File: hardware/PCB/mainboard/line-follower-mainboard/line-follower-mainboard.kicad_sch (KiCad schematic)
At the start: 29 parts, among them J1 Xt30, J2 2-Pin, J3 2-Pin, J4 8x2 Sensor connector, U2 L7805, U3 74HC164

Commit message: Created prototype sensor array schematic and PCB, revised mainboard
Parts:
- J4: footprint (none) -> Connector_PinSocket_2.54mm:PinSocket_2x08_P2.54mm_Vertical; DigiKeyPartNumber (none) -> S7111-ND

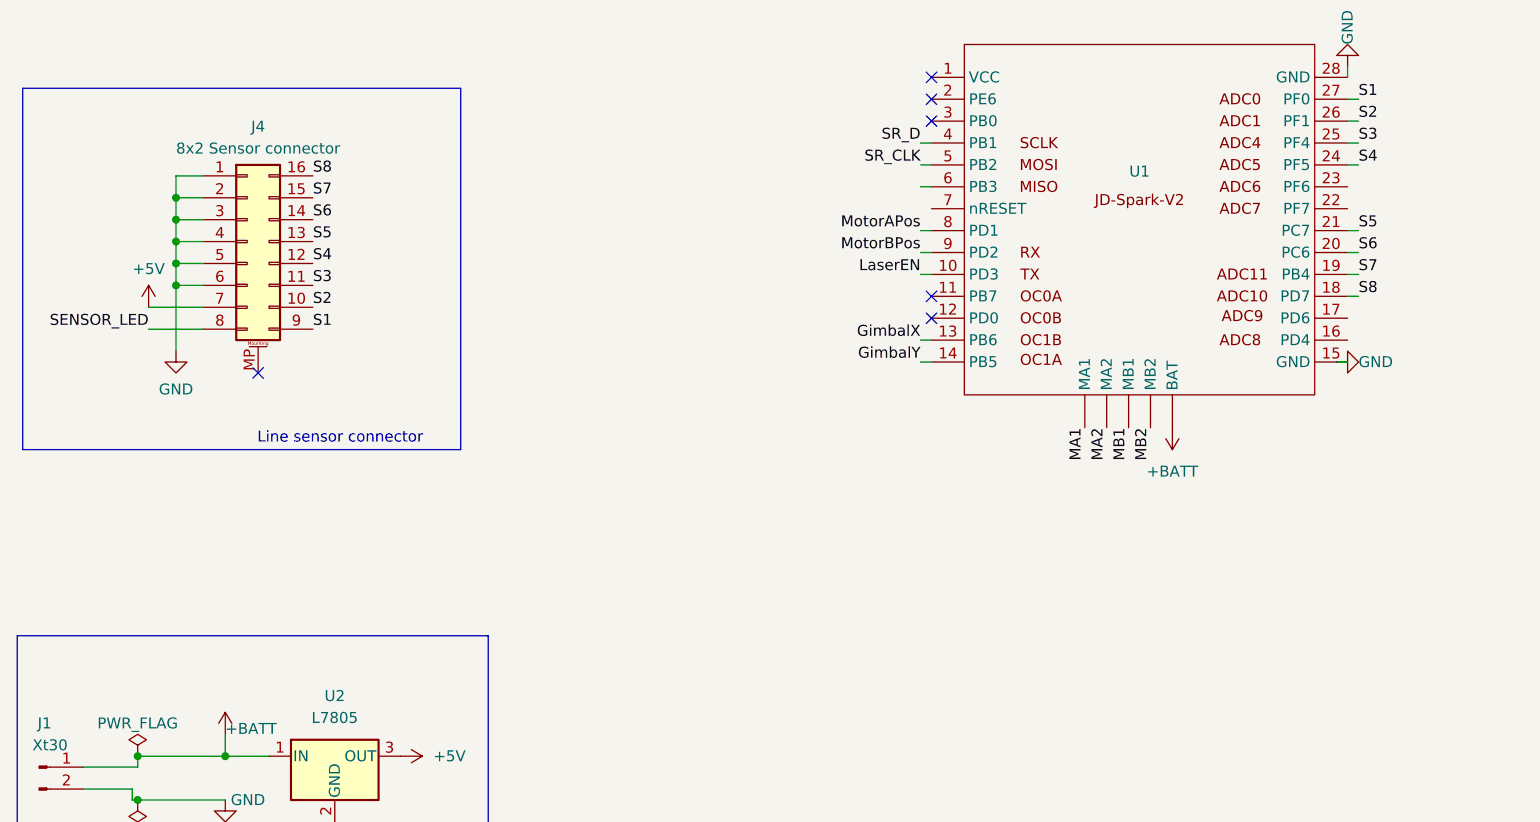
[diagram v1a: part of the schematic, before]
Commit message: Finished PCBs for payload and turret
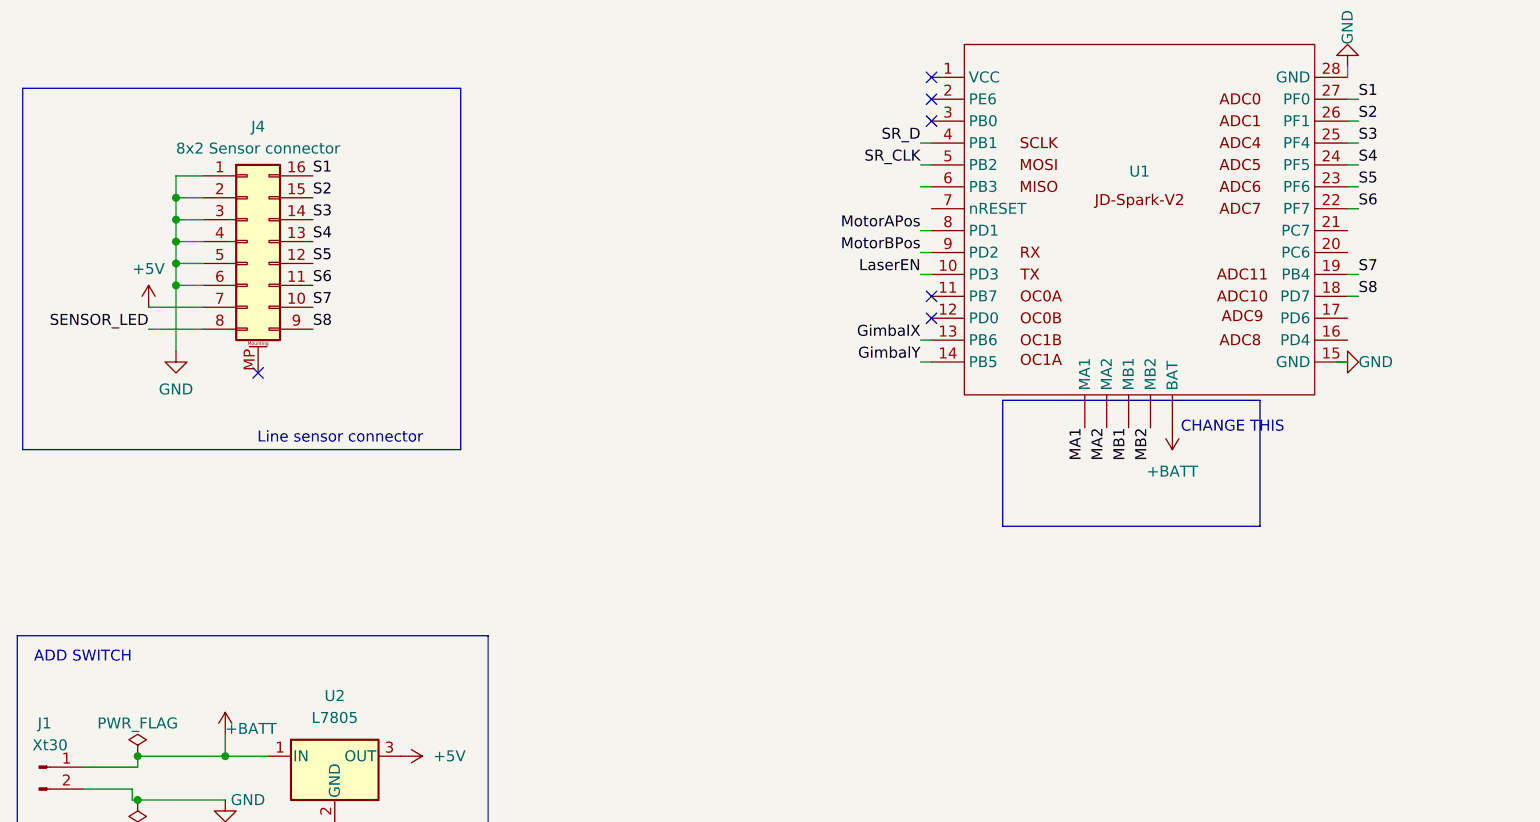
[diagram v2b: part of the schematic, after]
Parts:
- U3: DigiKeyPartNumber (none) -> 296-14838-1-ND
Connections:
- net S1: now also J4.16 (Pin_16); no longer J4.9 (Pin_9)
- net S2: now also J4.15 (Pin_15); no longer J4.10 (Pin_10)
- net S3: now also J4.14 (Pin_14); no longer J4.11 (Pin_11)
- net S4: now also J4.13 (Pin_13); no longer J4.12 (Pin_12)
- net S5: now also J4.12 (Pin_12), U1.23 (PF6); no longer J4.13 (Pin_13), U1.21 (PC7)
- net S6: now also J4.11 (Pin_11), U1.22 (PF7); no longer J4.14 (Pin_14), U1.20 (PC6)
- net S7: now also J4.10 (Pin_10); no longer J4.15 (Pin_15)
- net S8: now also J4.9 (Pin_9); no longer J4.16 (Pin_16)
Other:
- note added: "ADD SWITCH"
- note added: "CHANGE THIS"

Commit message: payload v2
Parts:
- removed D1, D10, D2, D3, D4, D7, D8, D9: 1N5817, symbol Device:D_Schottky
- removed D11, D12, D5, D6: LED, symbol Device:LED
- removed J2, J3: 2-Pin, symbol Connector:Conn_01x02_Pin
- removed R1, R2, R3: 150R, symbol Device:R
- removed U1: ~, symbol MCU_Microchip_ATmega:JD-Spark-V2
- added D4: STATUS, LED_THT:LED_D5.0mm, symbol Device:LED
- added H1, H2, H3, H4: MountingHole, MountingHole:MountingHole_3.2mm_M3_DIN965_Pad_TopBottom, symbol Mechanical:MountingHole_Pad
- added J3: linefollower->payload, Connector_PinHeader_2.54mm:PinHeader_2x08_P2.54mm_Vertical, symbol Connector_Generic:Conn_01x07
- added J4: MOTOR_B, Connector_PinHeader_2.54mm:PinHeader_1x02_P2.54mm_Vertical, symbol Connector:Screw_Terminal_01x02
- added J5: MOTOR_A, Connector_PinHeader_2.54mm:PinHeader_1x02_P2.54mm_Vertical, symbol Connector:Screw_Terminal_01x02
- added SW1: RST, symbol Switch:SW_Push
- added SW2: MODE, symbol Switch:SW_Push
- added U3: Teensy2.0_(Arduino), Library:Teensy2.0, symbol teensy:Teensy2.0_(Arduino)
- added U4: ~, Library:DRV8833, symbol Driver_Motor:DRV8833
- D1: renamed from D13; footprint (none) -> LED_THT:LED_D5.0mm
- D2: renamed from D14; footprint (none) -> LED_THT:LED_D5.0mm
- D3: renamed from D15; footprint (none) -> LED_THT:LED_D5.0mm
- J1: footprint (none) -> Connector_AMASS:AMASS_XT30PW-M_1x02_P2.50mm_Horizontal
- R1: renamed from R5; footprint (none) -> Resistor_THT:R_Axial_DIN0207_L6.3mm_D2.5mm_P7.62mm_Horizontal
- R2: renamed from R6; footprint (none) -> Resistor_THT:R_Axial_DIN0207_L6.3mm_D2.5mm_P7.62mm_Horizontal
- R3: renamed from R7; footprint (none) -> Resistor_THT:R_Axial_DIN0207_L6.3mm_D2.5mm_P7.62mm_Horizontal
- R4: value 150R -> 100; footprint (none) -> Resistor_THT:R_Axial_DIN0207_L6.3mm_D2.5mm_P7.62mm_Horizontal
- U2: renamed from U3; footprint (none) -> Library:74HC164DR
- renumbered J4 to J2, U2 to U1
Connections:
- net MB2 is gone; now on net Q3: R4.2
- net GND: now also D4.1 (K), H1.1, H2.1, H3.1, H4.1, J3.1 (Pin_1), J3.7 (Pin_7), SW1.2, SW2.1, U3.1 (GND), U3.15 (GND), U4.1 (GND), U4.9 (GND)
- net S1: now also U3.28 (21_A0)
- net S2: now also U3.27 (20_A1)
- net S3: now also U3.26 (19_A2)
- net S4: now also U3.25 (18_A3)
- net S5: now also U3.24 (17_A4)
- net S6: now also U3.23 (16_A5)
- net S7: now also U3.22 (15_A6_PWM)
- net S8: now also U3.21 (14_A7_PWM)
- net SR_CLK: now also U3.3 (1)
- net SR_D: now also U3.2 (0)
- net at R4.1: now also D4.2 (A)
- net Q3: now reaches U2.6 (Q3)
- net +5V renamed 5V
- net 5V: now also J3.2 (Pin_2), J3.6 (Pin_6), U3.14 (+5V)
- net +BATT renamed VBATT
- net VBATT: now also J3.4 (Pin_4), U4.2 (VIN)
- new net: J5.1 (Pin_1), U4.13 (AOUT2)
- new net: J5.2 (Pin_2), U4.14 (AOUT1)
- new net: SW2.2, U3.17 (22_A11)
- new net: SW1.1, U3.16 (RST)
- new net: J4.1 (Pin_1), U4.11 (BOUT1)
- new net: J4.2 (Pin_2), U4.12 (BOUT2)
- new net MOT_A1_PWM: U3.12 (10_PWM), U4.6 (AIN1)
- new net MOT_A2_PWM: U3.11 (9_PWM), U4.5 (AIN2)
- new net MOT_B1_PWM: U3.6 (4_PWM), U4.3 (BIN1)
- new net MOT_B2_PWM: U3.7 (5_INT0_PWM), U4.4 (BIN2)
- new net MOT_FLT: U3.13 (23), U4.8 (nFAULT)
- new net SZ_SIG: J3.5 (Pin_5), U3.4 (2)
- new net TRK_SIG: J3.3 (Pin_3), U3.5 (3)
- no-connect marks 6 -> 17
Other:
- note removed: "CHANGE THIS"
- note removed: "Motor A and B"

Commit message: finalised mainboard design
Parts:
- removed J2: 8x2 Sensor connector, Connector_PinSocket_2.54mm:PinSocket_2x08_P2.54mm_Vertical, symbol Connector_Generic_MountingPin:Conn_02x08_Counter_Clockwise_MountingPin
- removed SW1: RST, symbol Switch:SW_Push
- removed SW2: MODE, symbol Switch:SW_Push
- added J2: Conn_02x08_Odd_Even, Connector_PinHeader_2.54mm:PinHeader_2x08_P2.54mm_Vertical, symbol Connector_Generic:Conn_02x08_Odd_Even
- added SW1: RST, footprints:SO4_222A-M-V-B_CTS, symbol Switch:SW_MEC_5E
- added SW2: MODE, footprints:SO4_222A-M-V-B_CTS, symbol Switch:SW_MEC_5E
- J3: footprint Connector_PinHeader_2.54mm:PinHeader_2x08_P2.54mm_Vertical -> Connector_PinHeader_2.54mm:PinHeader_1x07_P2.54mm_Vertical
- U2: footprint Library:74HC164DR -> footprints:D14
- U3: footprint Library:Teensy2.0 -> footprints:Teensy2.0
- U4: footprint Library:DRV8833 -> footprints:DRV8833
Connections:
- net 5V: now also J2.13 (Pin_13)
- net GND: now also J2.1 (Pin_1), J2.11 (Pin_11), J2.3 (Pin_3), J2.5 (Pin_5), J2.7 (Pin_7), J2.9 (Pin_9), SW1.1, SW1.2, SW2.3 (K), SW2.4 (A)
- net Q0: now also U3.2 (0)
- net Q1: now also U3.3 (1)
- net Q2: now also U3.4 (2)
- net Q3: now also U3.5 (3)
- net S1: now also U3.21 (14_A7_PWM), J2.2 (Pin_2); no longer U3.28 (21_A0)
- net S2: now also U3.22 (15_A6_PWM), J2.4 (Pin_4); no longer U3.27 (20_A1)
- net S3: now also U3.23 (16_A5), J2.6 (Pin_6); no longer U3.26 (19_A2)
- net S4: now also U3.24 (17_A4), J2.8 (Pin_8); no longer U3.25 (18_A3)
- net S5: now also U3.25 (18_A3), J2.10 (Pin_10); no longer U3.24 (17_A4)
- net S6: now also U3.26 (19_A2), J2.12 (Pin_12); no longer U3.23 (16_A5)
- net S7: now also U3.27 (20_A1), J2.14 (Pin_14); no longer U3.22 (15_A6_PWM)
- net S8: now also U3.28 (21_A0), J2.16 (Pin_16); no longer U3.21 (14_A7_PWM)
- net SENSOR_LED: now also J2.15 (Pin_15)
- net SR_CLK: no longer U3.3 (1)
- net SR_D: no longer U3.2 (0)
- net SZ_SIG: now also U3.20 (13_A8); no longer U3.4 (2)
- net TRK_SIG: now also U3.19 (12_A9_PWM); no longer U3.5 (3)
- net at U3.17 (22_A11): now also SW2.1, SW2.2
- net at U3.16 (RST): now also SW1.3 (K), SW1.4 (A)
- no-connect marks 17 -> 14

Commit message: Code clean up, debug state added, state machine for payload added
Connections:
- net GND: now also J1.1 (Pin_1); no longer J1.2 (Pin_2)
- net VBATT: now also J1.2 (Pin_2); no longer J1.1 (Pin_1)
- no-connect marks 14 -> 12
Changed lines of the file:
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@@
 	)
 	(no_connect
-		(at 140.97 92.075)
-	)
-	(no_connect
 		(at 176.53 79.375)
 	)
 	(no_connect
-		(at 176.53 109.855)
-	)
-	(no_connect
 		(at 119.38 49.53)
 	)
@@
 	(wire
 		(pts
+			(xy 21.59 156.21) (xy 27.94 156.21)
+		)
+		(stroke
+			(width 0)
+			(type default)
+		)
+	)
+	(wire
+		(pts
 			(xy 171.45 125.73) (xy 176.53 125.73)
 		)
@@
 	(wire
 		(pts
-			(xy 21.59 156.21) (xy 27.94 156.21)
-		)
-		(stroke
-			(width 0)
-			(type default)
-		)
-	)
-	(wire
-		(pts
 			(xy 179.705 86.995) (xy 176.53 86.995)
 		)
@@
 	(symbol
 		(lib_id "Connector:Conn_01x02_Pin")
-		(at 16.51 156.21 0)
+		(at 16.51 158.75 0)
+		(mirror x)
 		(unit 1)
 		(exclude_from_sim no)
@@
 		(dnp no)
 		(property "Reference" "J1"
-			(at 17.145 151.13 0)
+			(at 17.145 163.83 0)
 			(effects
 				(font
@@
 		)
 		(property "Value" "Xt30"
-			(at 17.78 153.67 0)
+			(at 17.78 161.29 0)
 			(effects
 				(font
@@
 		)
 		(property "Footprint" "Connector_AMASS:AMASS_XT30PW-M_1x02_P2.50mm_Horizontal"
-			(at 16.51 156.21 0)
+			(at 16.51 158.75 0)
 			(effects
 				(font
@@
 		)
 		(property "Datasheet" "~"
-			(at 16.51 156.21 0)
+			(at 16.51 158.75 0)
 			(effects
 				(font
@@
 		)
 		(property "Description" "Generic connector, single row, 01x02, script generated"
-			(at 16.51 156.21 0)
+			(at 16.51 158.75 0)
 			(effects
 				(font
@@
 		)
 		(property "DigiKeyPartNumber" ""
-			(at 16.51 156.21 0)
+			(at 16.51 158.75 0)
 			(effects
 				(font

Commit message: Final project commit
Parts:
- removed U2: 74HC164, footprints:D14, symbol 74xx:74HC164
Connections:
- no-connect marks 12 -> 9
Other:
- company: (none) -> Designed by Maurice Blake
- title: (none) -> Line Follower Mainboard
